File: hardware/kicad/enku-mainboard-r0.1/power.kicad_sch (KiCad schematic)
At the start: 42 parts

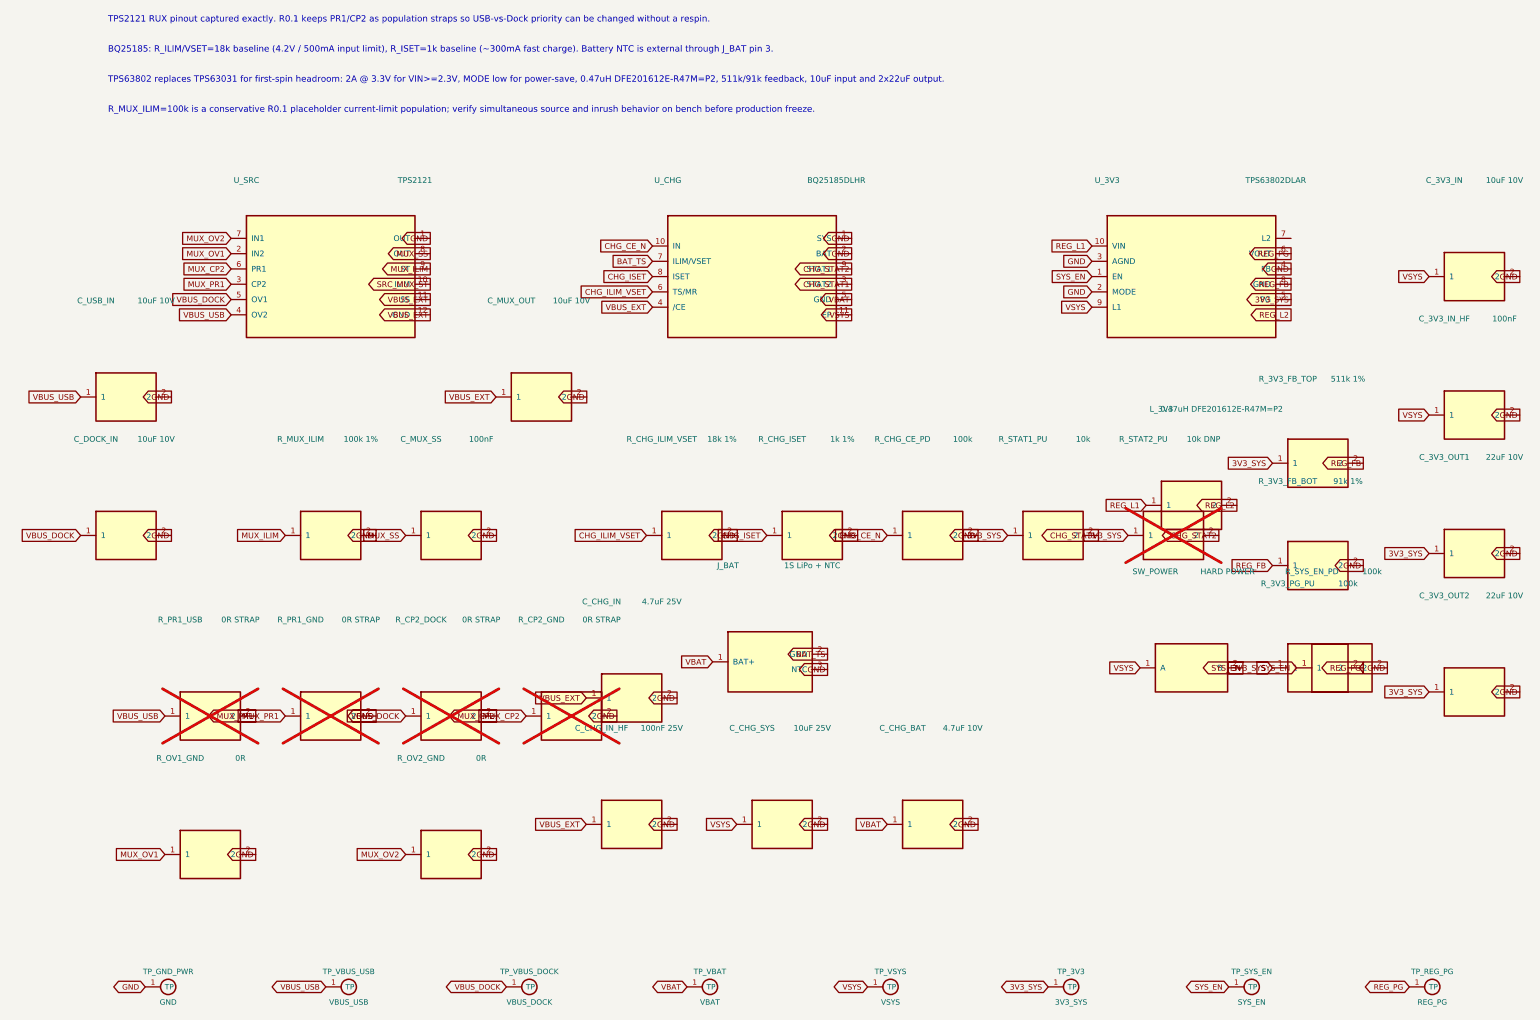
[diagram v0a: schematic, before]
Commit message: Fix KiCad pin-label Y transform in power
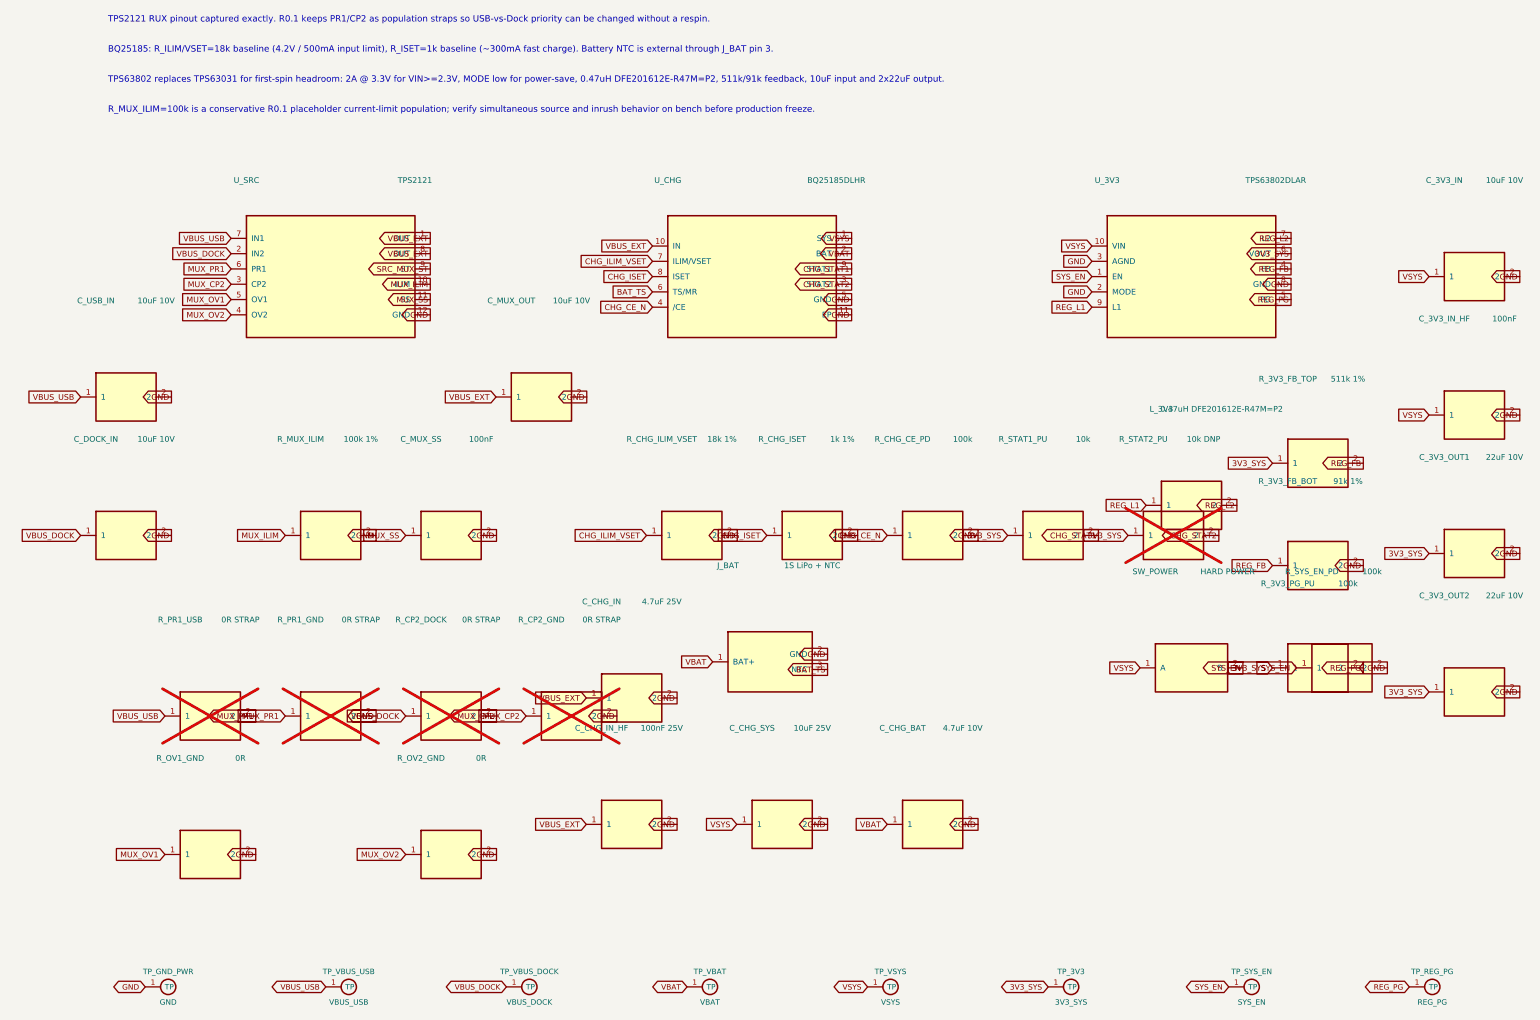
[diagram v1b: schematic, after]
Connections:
- net 3V3_SYS: now also U_3V3.6 (VOUT); no longer U_3V3.5 (PG)
- net BAT_TS: now also J_BAT.3 (NTC), U_CHG.6 (TS/MR); no longer J_BAT.2 (GND), U_CHG.7 (ILIM/VSET)
- net CHG_CE_N: now also U_CHG.4 (/CE); no longer U_CHG.10 (IN)
- net CHG_ILIM_VSET: now also U_CHG.7 (ILIM/VSET); no longer U_CHG.6 (TS/MR)
- net CHG_STAT1: now also U_CHG.9 (STAT1); no longer U_CHG.3 (STAT2)
- net CHG_STAT2: now also U_CHG.3 (STAT2); no longer U_CHG.9 (STAT1)
- net GND: now also J_BAT.2 (GND), U_3V3.8 (GND), U_CHG.11 (EP), U_CHG.5 (GND), U_SRC.12 (GND); no longer J_BAT.3 (NTC), U_3V3.4 (FB), U_CHG.1 (SYS), U_CHG.2 (BAT), U_SRC.1 (OUT)
- net MUX_CP2: now also U_SRC.3 (CP2); no longer U_SRC.6 (PR1)
- net MUX_ILIM: now also U_SRC.10 (ILIM); no longer U_SRC.9 (ST)
- net MUX_OV1: now also U_SRC.5 (OV1); no longer U_SRC.2 (IN2)
- net MUX_OV2: now also U_SRC.4 (OV2); no longer U_SRC.7 (IN1)
- net MUX_PR1: now also U_SRC.6 (PR1); no longer U_SRC.3 (CP2)
- net MUX_SS: now also U_SRC.11 (SS); no longer U_SRC.8 (OUT)
- net REG_FB: now also U_3V3.4 (FB); no longer U_3V3.8 (GND)
- net REG_L1: now also U_3V3.9 (L1); no longer U_3V3.10 (VIN)
- net REG_L2: now also U_3V3.7 (L2)
- net REG_PG: now also U_3V3.5 (PG); no longer U_3V3.6 (VOUT)
- net SRC_MUX_ST: now also U_SRC.9 (ST); no longer U_SRC.10 (ILIM)
- net VBAT: now also U_CHG.2 (BAT); no longer U_CHG.5 (GND)
- net VBUS_DOCK: now also U_SRC.2 (IN2); no longer U_SRC.5 (OV1)
- net VBUS_EXT: now also U_CHG.10 (IN), U_SRC.1 (OUT), U_SRC.8 (OUT); no longer U_CHG.4 (/CE), U_SRC.11 (SS), U_SRC.12 (GND)
- net VBUS_USB: now also U_SRC.7 (IN1); no longer U_SRC.4 (OV2)
- net VSYS: now also U_3V3.10 (VIN), U_CHG.1 (SYS); no longer U_3V3.9 (L1), U_CHG.11 (EP)
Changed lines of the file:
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@@
 		(instances (project "enku-mainboard-r0.1" (path "/10000000-0000-4000-8000-000000000001/10000000-0000-4000-8000-000000000010" (reference "U_SRC") (unit 1))))
 	)
-	(global_label "VBUS_EXT" (shape output) (at 78.53999999999999 68.35 180) (effects (font (size 0.95 0.95)) (justify right bottom)))
-	(global_label "VBUS_DOCK" (shape input) (at 45.46 65.80999999999999 0) (effects (font (size 0.95 0.95)) (justify right bottom)))
-	(global_label "MUX_CP2" (shape input) (at 45.46 60.73 0) (effects (font (size 0.95 0.95)) (justify right bottom)))
-	(global_label "MUX_OV2" (shape input) (at 45.46 55.64999999999999 0) (effects (font (size 0.95 0.95)) (justify right bottom)))
-	(global_label "MUX_OV1" (shape input) (at 45.46 58.19 0) (effects (font (size 0.95 0.95)) (justify right bottom)))
-	(global_label "MUX_PR1" (shape input) (at 45.46 63.269999999999996 0) (effects (font (size 0.95 0.95)) (justify right bottom)))
-	(global_label "VBUS_USB" (shape input) (at 45.46 68.35 0) (effects (font (size 0.95 0.95)) (justify right bottom)))
-	(global_label "VBUS_EXT" (shape output) (at 78.53999999999999 65.80999999999999 180) (effects (font (size 0.95 0.95)) (justify right bottom)))
-	(global_label "SRC_MUX_ST" (shape output) (at 78.53999999999999 63.269999999999996 180) (effects (font (size 0.95 0.95)) (justify right bottom)))
-	(global_label "MUX_ILIM" (shape output) (at 78.53999999999999 60.73 180) (effects (font (size 0.95 0.95)) (justify right bottom)))
-	(global_label "MUX_SS" (shape output) (at 78.53999999999999 58.19 180) (effects (font (size 0.95 0.95)) (justify right bottom)))
-	(global_label "GND" (shape output) (at 78.53999999999999 55.64999999999999 180) (effects (font (size 0.95 0.95)) (justify right bottom)))
+	(global_label "VBUS_EXT" (shape output) (at 78.54 55.65 180) (effects (font (size 0.95 0.95)) (justify right bottom)))
+	(global_label "VBUS_DOCK" (shape input) (at 45.46 58.19 0) (effects (font (size 0.95 0.95)) (justify right bottom)))
+	(global_label "MUX_CP2" (shape input) (at 45.46 63.27 0) (effects (font (size 0.95 0.95)) (justify right bottom)))
+	(global_label "MUX_OV2" (shape input) (at 45.46 68.35 0) (effects (font (size 0.95 0.95)) (justify right bottom)))
+	(global_label "MUX_OV1" (shape input) (at 45.46 65.81 0) (effects (font (size 0.95 0.95)) (justify right bottom)))
+	(global_label "MUX_PR1" (shape input) (at 45.46 60.73 0) (effects (font (size 0.95 0.95)) (justify right bottom)))
+	(global_label "VBUS_USB" (shape input) (at 45.46 55.65 0) (effects (font (size 0.95 0.95)) (justify right bottom)))
+	(global_label "VBUS_EXT" (shape output) (at 78.54 58.19 180) (effects (font (size 0.95 0.95)) (justify right bottom)))
+	(global_label "SRC_MUX_ST" (shape output) (at 78.54 60.73 180) (effects (font (size 0.95 0.95)) (justify right bottom)))
+	(global_label "MUX_ILIM" (shape output) (at 78.54 63.27 180) (effects (font (size 0.95 0.95)) (justify right bottom)))
+	(global_label "MUX_SS" (shape output) (at 78.54 65.81 180) (effects (font (size 0.95 0.95)) (justify right bottom)))
+	(global_label "GND" (shape output) (at 78.54 68.35 180) (effects (font (size 0.95 0.95)) (justify right bottom)))
 	(symbol (lib_id "ENKU:BQ25185_DLH") (at 132 62 0) (unit 1) (exclude_from_sim no) (in_bom yes) (on_board yes) (dnp no)
 		(property "Reference" "U_CHG" (at 118 46 0) (effects (font (size 0.95 0.95))))
@@
 		(instances (project "enku-mainboard-r0.1" (path "/10000000-0000-4000-8000-000000000001/10000000-0000-4000-8000-000000000010" (reference "U_CHG") (unit 1))))
 	)
-	(global_label "VSYS" (shape output) (at 148.54 68.35 180) (effects (font (size 0.95 0.95)) (justify right bottom)))
-	(global_label "VBAT" (shape output) (at 148.54 65.80999999999999 180) (effects (font (size 0.95 0.95)) (justify right bottom)))
-	(global_label "CHG_STAT2" (shape output) (at 148.54 60.73 180) (effects (font (size 0.95 0.95)) (justify right bottom)))
-	(global_label "CHG_CE_N" (shape input) (at 115.46000000000001 56.92 0) (effects (font (size 0.95 0.95)) (justify right bottom)))
-	(global_label "GND" (shape output) (at 148.54 58.19 180) (effects (font (size 0.95 0.95)) (justify right bottom)))
-	(global_label "BAT_TS" (shape input) (at 115.46000000000001 59.46 0) (effects (font (size 0.95 0.95)) (justify right bottom)))
-	(global_label "CHG_ILIM_VSET" (shape input) (at 115.46000000000001 64.53999999999999 0) (effects (font (size 0.95 0.95)) (justify right bottom)))
+	(global_label "VSYS" (shape output) (at 148.54 55.65 180) (effects (font (size 0.95 0.95)) (justify right bottom)))
+	(global_label "VBAT" (shape output) (at 148.54 58.19 180) (effects (font (size 0.95 0.95)) (justify right bottom)))
+	(global_label "CHG_STAT2" (shape output) (at 148.54 63.27 180) (effects (font (size 0.95 0.95)) (justify right bottom)))
+	(global_label "CHG_CE_N" (shape input) (at 115.46 67.08 0) (effects (font (size 0.95 0.95)) (justify right bottom)))
+	(global_label "GND" (shape output) (at 148.54 65.81 180) (effects (font (size 0.95 0.95)) (justify right bottom)))
+	(global_label "BAT_TS" (shape input) (at 115.46 64.54 0) (effects (font (size 0.95 0.95)) (justify right bottom)))
+	(global_label "CHG_ILIM_VSET" (shape input) (at 115.46 59.46 0) (effects (font (size 0.95 0.95)) (justify right bottom)))
 	(global_label "CHG_ISET" (shape input) (at 115.46000000000001 62 0) (effects (font (size 0.95 0.95)) (justify right bottom)))
-	(global_label "CHG_STAT1" (shape output) (at 148.54 63.269999999999996 180) (effects (font (size 0.95 0.95)) (justify right bottom)))
-	(global_label "VBUS_EXT" (shape input) (at 115.46000000000001 67.08 0) (effects (font (size 0.95 0.95)) (justify right bottom)))
-	(global_label "GND" (shape output) (at 148.54 55.64999999999999 180) (effects (font (size 0.95 0.95)) (justify right bottom)))
+	(global_label "CHG_STAT1" (shape output) (at 148.54 60.73 180) (effects (font (size 0.95 0.95)) (justify right bottom)))
+	(global_label "VBUS_EXT" (shape input) (at 115.46 56.92 0) (effects (font (size 0.95 0.95)) (justify right bottom)))
+	(global_label "GND" (shape output) (at 148.54 68.35 180) (effects (font (size 0.95 0.95)) (justify right bottom)))
 	(symbol (lib_id "ENKU:TPS63802_DLA") (at 205 62 0) (unit 1) (exclude_from_sim no) (in_bom yes) (on_board yes) (dnp no)
 		(property "Reference" "U_3V3" (at 191 46 0) (effects (font (size 0.95 0.95))))
@@
 		(instances (project "enku-mainboard-r0.1" (path "/10000000-0000-4000-8000-000000000001/10000000-0000-4000-8000-000000000010" (reference "U_3V3") (unit 1))))
 	)
-	(global_label "3V3_SYS" (shape output) (at 221.54 65.80999999999999 180) (effects (font (size 0.95 0.95)) (justify right bottom)))
-	(global_label "REG_L2" (shape output) (at 221.54 68.35 180) (effects (font (size 0.95 0.95)) (justify right bottom)))
-	(global_label "REG_PG" (shape output) (at 221.54 58.19 180) (effects (font (size 0.95 0.95)) (justify right bottom)))
-	(global_label "REG_L1" (shape input) (at 188.46 56.92 0) (effects (font (size 0.95 0.95)) (justify right bottom)))
-	(global_label "VSYS" (shape input) (at 188.46 67.08 0) (effects (font (size 0.95 0.95)) (justify right bottom)))
+	(global_label "3V3_SYS" (shape output) (at 221.54 58.19 180) (effects (font (size 0.95 0.95)) (justify right bottom)))
+	(global_label "REG_L2" (shape output) (at 221.54 55.65 180) (effects (font (size 0.95 0.95)) (justify right bottom)))
+	(global_label "REG_PG" (shape output) (at 221.54 65.81 180) (effects (font (size 0.95 0.95)) (justify right bottom)))
+	(global_label "REG_L1" (shape input) (at 188.46 67.08 0) (effects (font (size 0.95 0.95)) (justify right bottom)))
+	(global_label "VSYS" (shape input) (at 188.46 56.92 0) (effects (font (size 0.95 0.95)) (justify right bottom)))
 	(global_label "SYS_EN" (shape input) (at 188.46 62 0) (effects (font (size 0.95 0.95)) (justify right bottom)))
+	(global_label "GND" (shape input) (at 188.46 64.54 0) (effects (font (size 0.95 0.95)) (justify right bottom)))
 	(global_label "GND" (shape input) (at 188.46 59.46 0) (effects (font (size 0.95 0.95)) (justify right bottom)))
-	(global_label "GND" (shape input) (at 188.46 64.53999999999999 0) (effects (font (size 0.95 0.95)) (justify right bottom)))
-	(global_label "GND" (shape output) (at 221.54 60.73 180) (effects (font (size 0.95 0.95)) (justify right bottom)))
-	(global_label "REG_FB" (shape output) (at 221.54 63.269999999999996 180) (effects (font (size 0.95 0.95)) (justify right bottom)))
+	(global_label "GND" (shape output) (at 221.54 63.27 180) (effects (font (size 0.95 0.95)) (justify right bottom)))
+	(global_label "REG_FB" (shape output) (at 221.54 60.73 180) (effects (font (size 0.95 0.95)) (justify right bottom)))
 	(symbol (lib_id "ENKU:BAT3") (at 135 126 0) (unit 1) (exclude_from_sim no) (in_bom yes) (on_board yes) (dnp no)
 		(property "Reference" "J_BAT" (at 128 110 0) (effects (font (size 0.95 0.95))))
@@
 	)
 	(global_label "VBAT" (shape input) (at 125.46000000000001 126 0) (effects (font (size 0.95 0.95)) (justify right bottom)))
-	(global_label "GND" (shape output) (at 144.54 127.27 180) (effects (font (size 0.95 0.95)) (justify right bottom)))
-	(global_label "BAT_TS" (shape output) (at 144.54 124.72999999999999 180) (effects (font (size 0.95 0.95)) (justify right bottom)))
+	(global_label "GND" (shape output) (at 144.54 124.73 180) (effects (font (size 0.95 0.95)) (justify right bottom)))
+	(global_label "BAT_TS" (shape output) (at 144.54 127.27 180) (effects (font (size 0.95 0.95)) (justify right bottom)))
 	(symbol (lib_id "ENKU:R") (at 62 105 0) (unit 1) (exclude_from_sim no) (in_bom yes) (on_board yes) (dnp no)
 		(property "Reference" "R_MUX_ILIM" (at 57 89 0) (effects (font (size 0.95 0.95))))
